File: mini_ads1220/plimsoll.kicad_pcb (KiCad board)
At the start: 4 copper layers, 16.3 x 29.1 mm, 17 parts, among them J1 Conn_02x06_Odd_Even, J3 Loadd Cell, U5 RS3236-3.3, U6 HX717

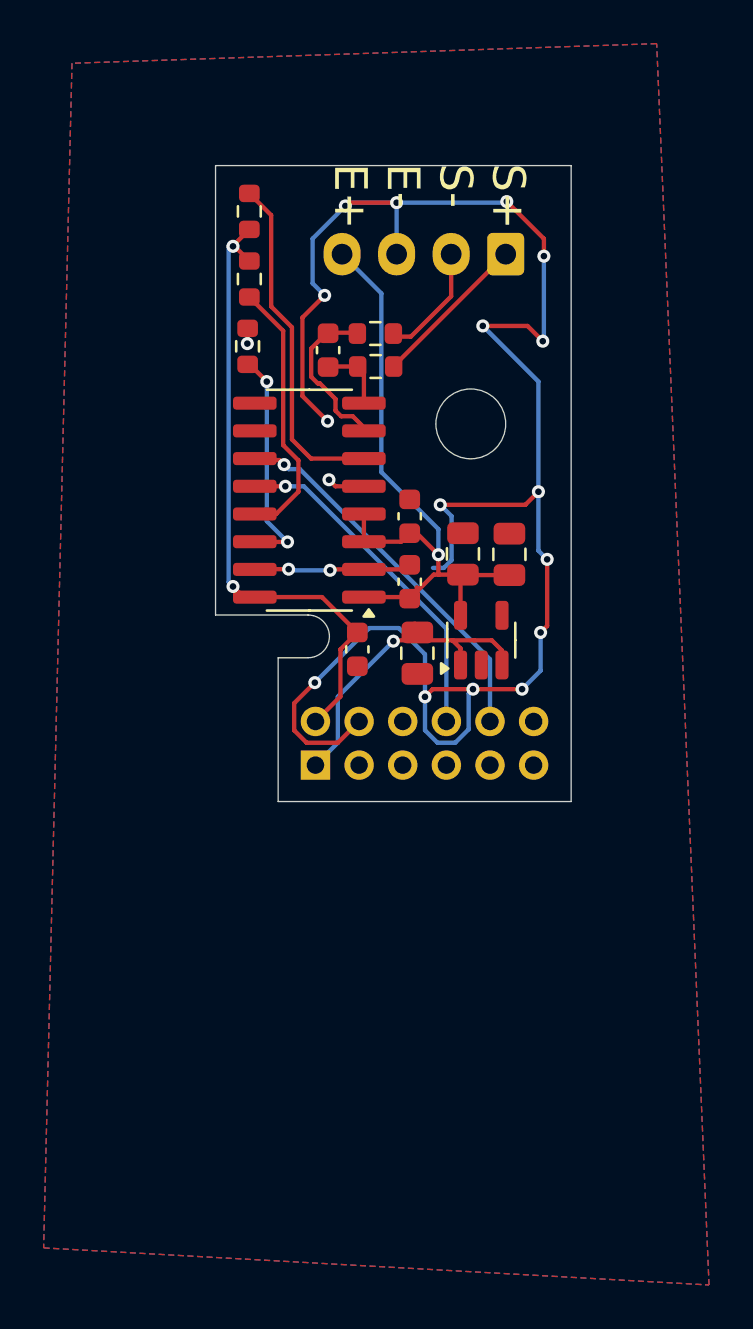
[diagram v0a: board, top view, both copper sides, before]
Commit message: ads1220 added
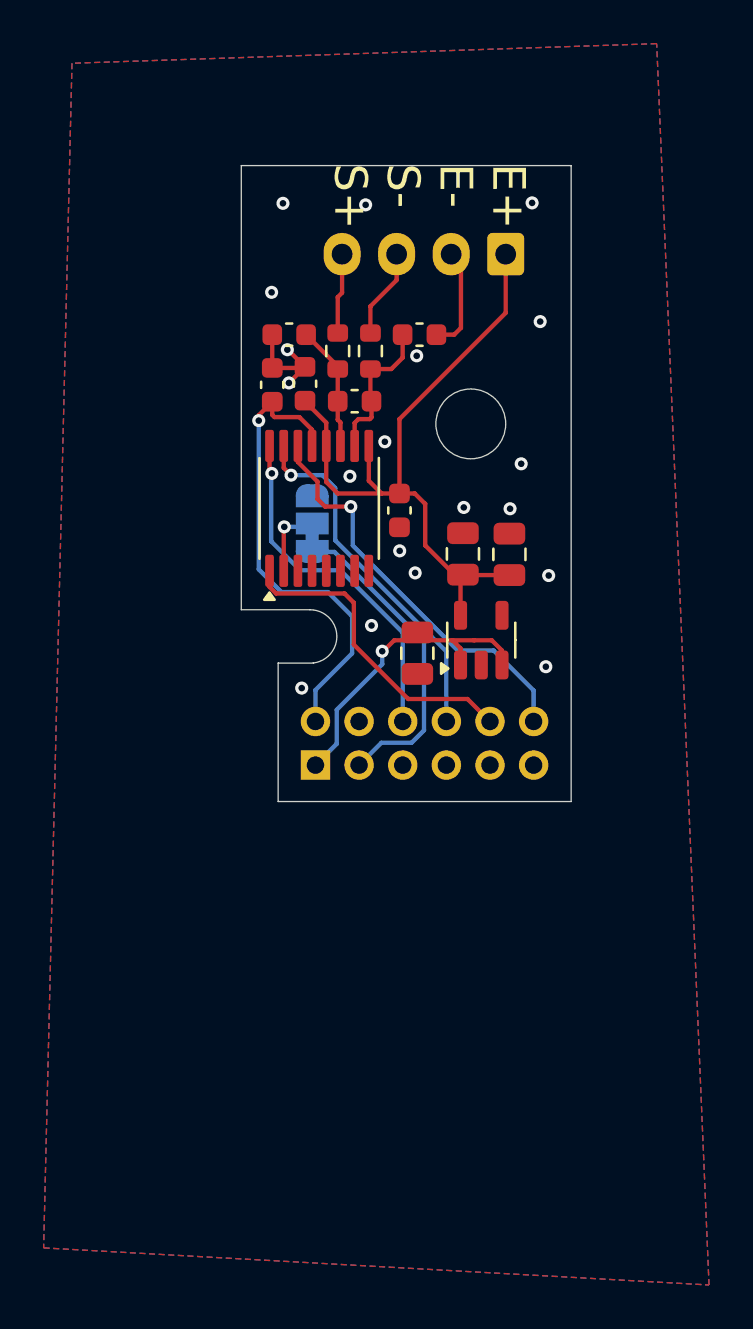
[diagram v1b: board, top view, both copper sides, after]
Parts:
- removed R10, R11, R12: 10k, Resistor_SMD:R_0603_1608Metric
- removed U6: HX717, Package_SO:SOP-16_3.9x9.9mm_P1.27mm
- added C1: DNP, Capacitor_SMD:C_0603_1608Metric, F.Cu at (34.2, 27.8)
- added C2: DNP, Capacitor_SMD:C_0603_1608Metric, F.Cu at (28.3, 27.8)
- added JP2: ~{CS}, Jumper:SolderJumper-3_P1.3mm_Bridged12_RoundedPad1.0x1.5mm_NumberLabels, B.Cu at (29.3, 36.4)
- added U1: ADS1220xPW, Package_SO:TSSOP-16_4.4x5mm_P0.65mm, F.Cu at (29.6, 35.7)
- moved C9 12.7 mm to (27.5, 30.1), turned to 90 degrees
- moved C12 10.3 mm to (29.0, 30.0)
- moved C7 2.64 mm to (31.3, 30.8), turned to 180 degrees
- moved R7 1.88 mm to (30.5, 28.5), turned to 90 degrees
- moved R8 0.83 mm to (32.0, 28.5), turned to 90 degrees
- moved C8 0.54 mm to (33.3, 35.8), turned to -90 degrees
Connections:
- J3 pad 1: /Signal+ -> +3.3VADC
- J3 pad 2: /Signal- -> GND
- J3 pad 3: GND -> /Signal-
- J3 pad 4: +3.3VADC -> /Signal+
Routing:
- net GND: track 95.9 -> 10.1 mm, vias 20 -> 19
- net /C13: track 0.00 -> 18.8 mm, vias 0 -> 1
- net /B5: track 0.00 -> 16.3 mm, vias 0 -> 1
- net Net-(U6-S0): track 15.7 -> 0.00 mm
- net /B6: track 0.00 -> 14.5 mm
- net Net-(U6-S1): track 12.3 -> 0.00 mm
- net Net-(U6-XI): track 10.5 -> 0.00 mm, vias 2 -> 0
- net +3V3: track 29.4 -> 22.1 mm, vias 2 -> 1
- net /Signal+: track 7.28 -> 3.70 mm
- net Net-(JP2-C): track 0.00 -> 3.37 mm, vias 0 -> 1
- net /B3: track 17.7 -> 14.8 mm, vias 1 -> 0
- net Net-(U1-AIN0/REFP1): track 3.16 -> 5.75 mm
- net +3.3VADC: track 31.2 -> 32.7 mm, vias 1 -> 0
- net /Signal-: track 5.41 -> 4.11 mm
- net Net-(U1-AIN1): track 7.58 -> 6.92 mm
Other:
- board size 16.3 x 29.1 mm -> 15.1 x 29.1 mm
- board text added: "CDS1220 Mini"
- board text added: "E+ E- S- S+"
- board text removed: "HX717 Mini"
- board text removed: "S+ S- E- E+"
